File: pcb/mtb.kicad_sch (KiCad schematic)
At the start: 24 parts, among them J1 Screw_Terminal_01x04, J2 PROG/DEBUG, SW1 SW_MEC_5E, U1 AMS1117-3.3, U2 SN75176AP, Y1 Crystal

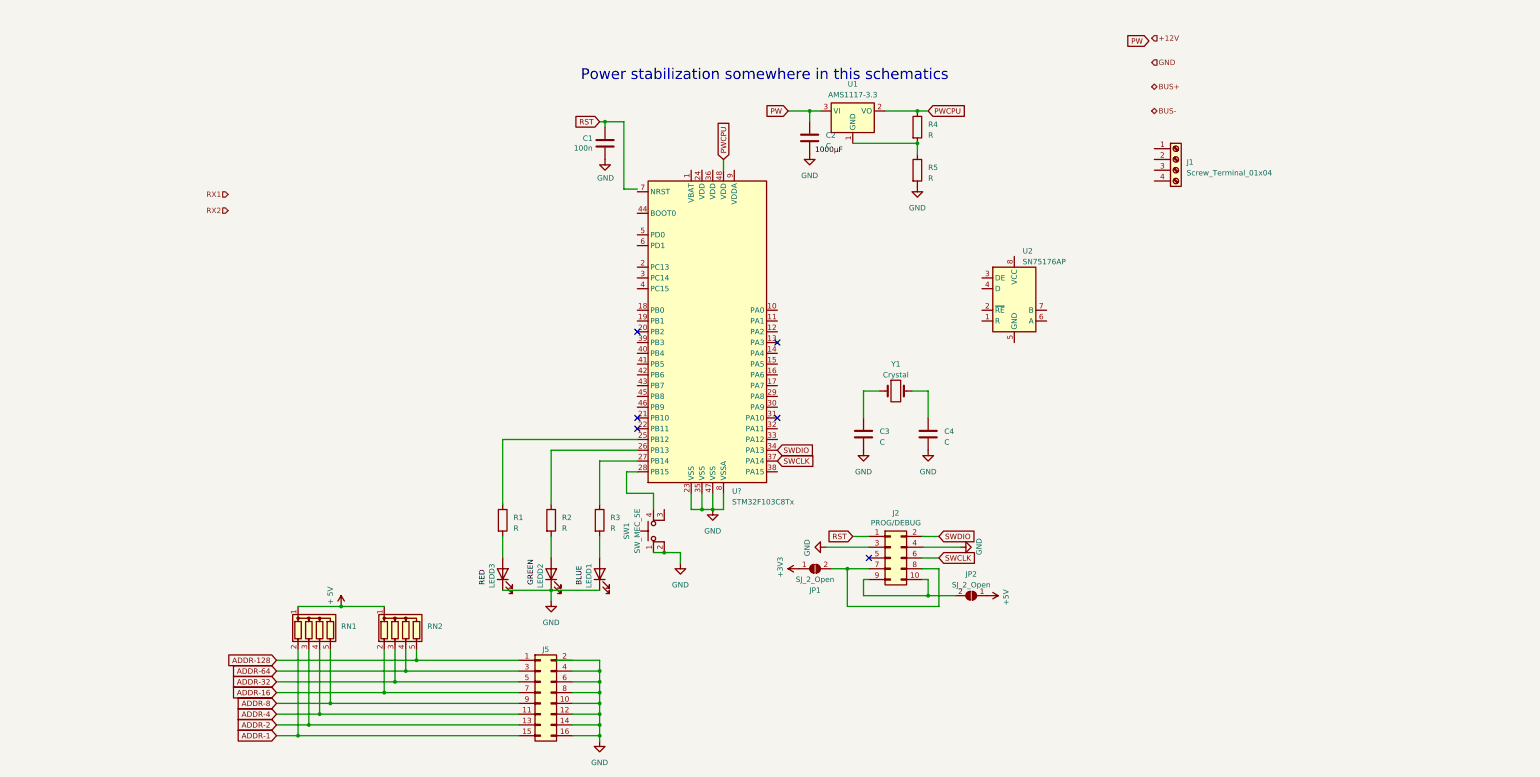
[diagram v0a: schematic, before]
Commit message: Wires adresses, add capacitors to MCU.
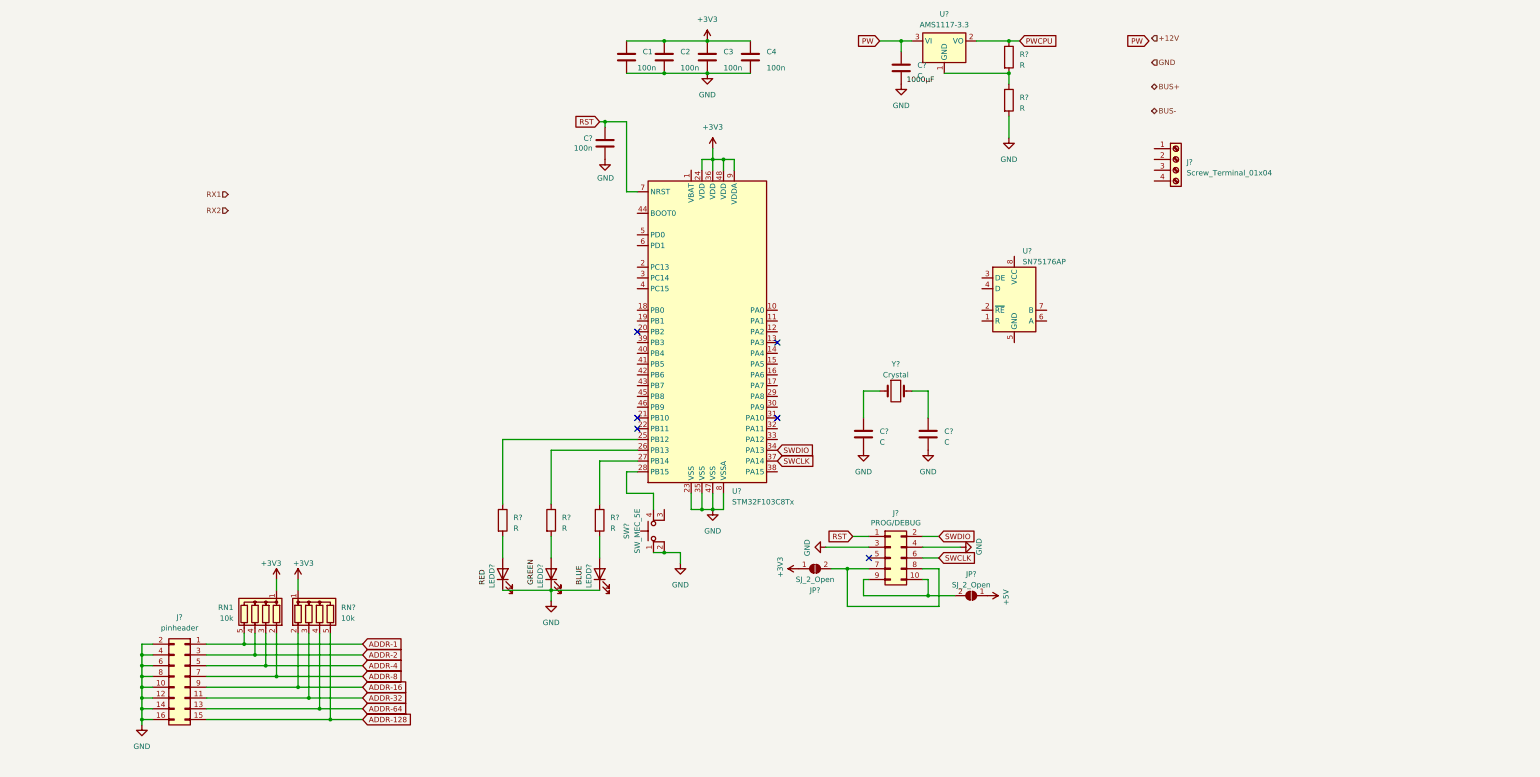
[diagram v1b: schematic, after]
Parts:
- removed RN2: R_Network04, Resistor_THT:R_Array_SIP5, symbol Device:R_Network04
- added C1, C2, C3, C4: 100n, symbol Device:C
- added RN?: 10k, Resistor_THT:R_Array_SIP5, symbol Device:R_Network04
- J?: renamed from J5; value ~ -> pinheader
- RN1: value R_Network04 -> 10k; footprint OptoDevice:R_LDR_5.1x4.3mm_P3.4mm_Vertical -> Resistor_THT:R_Array_SIP5
- renumbered C4 to C?, C2 to C?, C1 to C?, C3 to C?, D2 to D?, D3 to D?, D1 to D?, J2 to J?, J1 to J?, JP2 to JP?, JP1 to JP?, R2 to R?, R5 to R?, R4 to R?, R3 to R?, R1 to R?, SW1 to SW?, U2 to U?, U1 to U?, Y1 to Y?
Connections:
- net NEUT is gone; now on net +3V3: RN1.1 (common)
- net +3V3: now also U?.24 (VDD), U?.36 (VDD), U?.48 (VDD), U?.9 (VDDA), C1.1, C2.1, C3.1, C4.1, RN?.1 (common)
- net ADDR-1: now also J?.1 (Pin_1), RN1.5 (R4); no longer J?.15 (Pin_15), RN1.2 (R1)
- net ADDR-128: now also J?.15 (Pin_15), RN?.5 (R4); no longer J?.1 (Pin_1)
- net ADDR-16: now also J?.9 (Pin_9), RN?.2 (R1); no longer J?.7 (Pin_7)
- net ADDR-2: now also J?.3 (Pin_3), RN1.4 (R3); no longer J?.13 (Pin_13), RN1.3 (R2)
- net ADDR-32: now also J?.11 (Pin_11), RN?.3 (R2); no longer J?.5 (Pin_5)
- net ADDR-4: now also J?.5 (Pin_5), RN1.3 (R2); no longer J?.11 (Pin_11), RN1.4 (R3)
- net ADDR-64: now also J?.13 (Pin_13), RN?.4 (R3); no longer J?.3 (Pin_3)
- net ADDR-8: now also J?.7 (Pin_7), RN1.2 (R1); no longer J?.9 (Pin_9), RN1.5 (R4)
- net GND: now also J?.2 (Pin_2), C1.2, C2.2, C3.2, C4.2
- net PWCPU: no longer U?.48 (VDD)
- net RST: now also U?.7 (NRST)
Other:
- note removed: "Power stabilization somewhere in this schematics"
- moved on the sheet: C?, J?, R?, U?

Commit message: Add power supply.
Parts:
- removed C?: C, symbol Device:C
- removed J?: Screw_Terminal_01x04, symbol Connector:Screw_Terminal_01x04
- removed R? (x2): R, symbol Device:R
- added C5, C6: 100n, symbol Device:C
- added C7, C9: 22u, symbol Device:C
- added C8: 22u/25V, symbol Device:C
- added D1: D_Schottky, symbol Device:D_Schottky
- added D2: BZX84C18, Package_TO_SOT_SMD:SOT-23, symbol Diode:BZX84Cxx
- added D3: BT148, symbol Device:Q_SCR_KAG
- added F1: 200mA, symbol Device:Polyfuse
- added R1: 2k2, symbol Device:R
- added U1: L78L05_SOT89, Package_TO_SOT_SMD:SOT-89-3, symbol Regulator_Linear:L78L05_SOT89
- C? (x2): value C -> 22p
- Y?: value Crystal -> 8MHz
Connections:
- net PWCPU is gone; now on net +3V3: U?.2 (VO)
- net +12V: now also F1.2
- net +3V3: now also C7.2
- net +5V: now also C9.2, U1.1 (OUT)
- net GND: now also U?.1 (GND), C5.2, C6.2, C7.1, C8.2, C9.1, D3.1 (K), R1.2, U1.2 (GND)
- net at U?.5 (PD0): now also C?.1, Y?.2
- net at U?.6 (PD1): now also C?.1, Y?.1
- net PW: no longer names the net of U?.3 (VI)
- net PW: now also C8.1, D1.1 (K), D2.3 (K), D3.2 (A), U1.3 (IN)
- new net: C6.1, D2.1 (A), D3.3 (G), R1.1
- new net: C5.1, D1.2 (A), F1.1
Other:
- moved on the sheet: C1, C2, C3, C4, C?, D?, J?, JP?, R?, SW?, U?, Y?

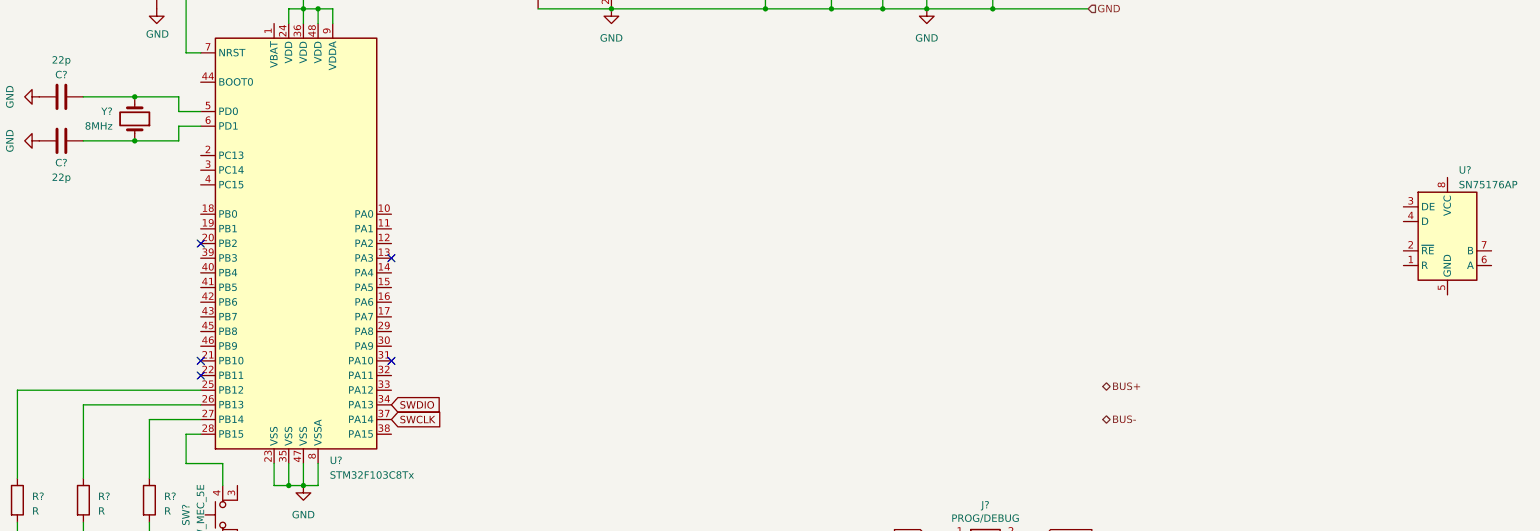
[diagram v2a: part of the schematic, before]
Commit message: Wire MTB bus driver.
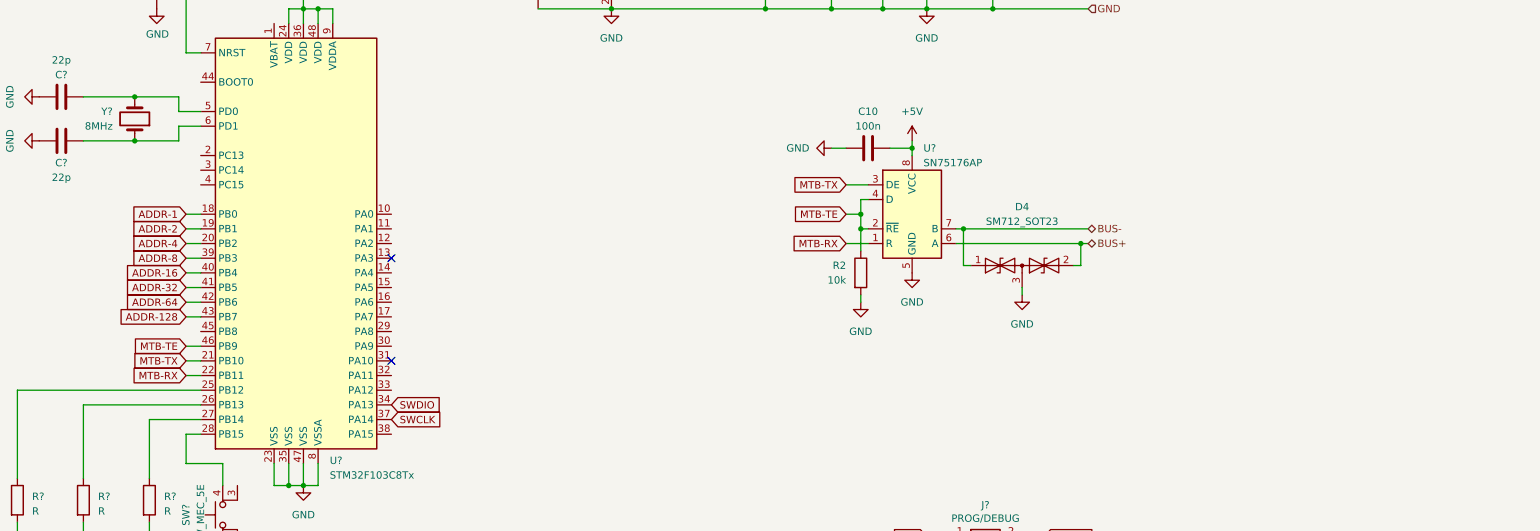
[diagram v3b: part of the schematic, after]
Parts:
- added C10: 100n, symbol Device:C
- added D4: SM712_SOT23, Package_TO_SOT_SMD:SOT-23, symbol Diode:SM712_SOT23
- added R2: 10k, symbol Device:R
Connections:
- net +5V: now also U?.8 (VCC), C10.1
- net ADDR-1: now also U?.18 (PB0)
- net ADDR-128: now also U?.43 (PB7)
- net ADDR-16: now also U?.40 (PB4)
- net ADDR-2: now also U?.19 (PB1)
- net ADDR-32: now also U?.41 (PB5)
- net ADDR-4: now also U?.20 (PB2)
- net ADDR-64: now also U?.42 (PB6)
- net ADDR-8: now also U?.39 (PB3)
- net BUS+: now also U?.6 (A), D4.2 (A2)
- net BUS-: now also U?.7 (B), D4.1 (A1)
- net GND: now also U?.5 (GND), C10.2, D4.3 (common), R2.2
- net MTB-TX: now reaches U?.21 (PB10)
- net MTB-TX: now also U?.3 (DE)
- net MTB-RX: now reaches U?.22 (PB11)
- net MTB-RX: now also U?.1 (R)
- net MTB-TE: now reaches U?.46 (PB9)
- net MTB-TE: now also U?.2 (~{RE}), U?.4 (D), R2.1
- no-connect marks 6 -> 3
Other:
- moved on the sheet: U?

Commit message: Finished MTB part.
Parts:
- added R2: 10k, symbol Device:R
- D1: renamed from D?; value LED -> BLUE
- D2: renamed from D?; value LED -> GREEN
- D3: renamed from D?; value LED -> RED
- R1, R3, R4: renamed from R?; value R -> 1k
- gave numbers to parts that had none: 13
- renumbered C4 to C1, C8 to C10, C10 to C11, C6 to C12, C5 to C13, C3 to C2, C2 to C3, C1 to C4, C9 to C8, C7 to C9, D3 to D4, D2 to D5, D1 to D6, D4 to D7, R2 to R5, R1 to R6, RN1 to RN2, U1 to U10
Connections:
- net GND: now also R2.2
- net RX1: now also U8.31 (PA10)
- net RX2: now also U8.13 (PA3)
- net DCC: now reaches U8.10 (PA0)
- net MULT1: now reaches U8.11 (PA1)
- net MULT2: now reaches U8.12 (PA2)
- net at U8.44 (BOOT0): now also R2.1
- no-connect marks 3 -> 16
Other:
- company: (none) -> Laboratory of railway vehicles control
- title: (none) -> RailComDet - MTB part
- moved on the sheet: C1, C11, C2, C3, C4, C5, C6, C7, D1, D2, D3, D7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

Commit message: DCC WIP.
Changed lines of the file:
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@@
     )
   )
-  (global_label "ADDR-16" (shape input) (at 218.44 144.78 180) (fields_autoplaced)
+  (global_label "ADDR-16" (shape output) (at 218.44 144.78 180) (fields_autoplaced)
     (effects (font (size 1.27 1.27)) (justify right))
-    (property "Intersheetrefs" "${INTERSHEET_REFS}" (at 206.6442 144.78 0)
+    (property "Intersheetrefs" "${INTERSHEET_REFS}" (at 206.5648 144.78 0)
       (effects (font (size 1.27 1.27)) (justify right) hide)
     )
@@
     )
   )
-  (global_label "ADDR-128" (shape input) (at 218.44 152.4 180) (fields_autoplaced)
+  (global_label "ADDR-128" (shape output) (at 218.44 152.4 180) (fields_autoplaced)
     (effects (font (size 1.27 1.27)) (justify right))
-    (property "Intersheetrefs" "${INTERSHEET_REFS}" (at 205.4347 152.4 0)
+    (property "Intersheetrefs" "${INTERSHEET_REFS}" (at 205.3553 152.4 0)
       (effects (font (size 1.27 1.27)) (justify right) hide)
     )
@@
     )
   )
-  (global_label "MTB-TX" (shape input) (at 88.9 113.03 0) (fields_autoplaced)
+  (global_label "MTB-TX" (shape output) (at 88.9 113.03 0) (fields_autoplaced)
     (effects (font (size 1.27 1.27)) (justify left))
     (property "Intersheetrefs" "${INTERSHEET_REFS}" (at 99.3237 113.03 0)
@@
     )
   )
-  (global_label "ADDR-1" (shape input) (at 218.44 134.62 180) (fields_autoplaced)
+  (global_label "ADDR-1" (shape output) (at 218.44 134.62 180) (fields_autoplaced)
     (effects (font (size 1.27 1.27)) (justify right))
-    (property "Intersheetrefs" "${INTERSHEET_REFS}" (at 207.8537 134.62 0)
+    (property "Intersheetrefs" "${INTERSHEET_REFS}" (at 207.7743 134.62 0)
       (effects (font (size 1.27 1.27)) (justify right) hide)
     )
@@
     )
   )
-  (global_label "ADDR-2" (shape input) (at 218.44 137.16 180) (fields_autoplaced)
+  (global_label "ADDR-2" (shape output) (at 218.44 137.16 180) (fields_autoplaced)
     (effects (font (size 1.27 1.27)) (justify right))
-    (property "Intersheetrefs" "${INTERSHEET_REFS}" (at 207.8537 137.16 0)
+    (property "Intersheetrefs" "${INTERSHEET_REFS}" (at 207.7743 137.16 0)
       (effects (font (size 1.27 1.27)) (justify right) hide)
     )
@@
     )
   )
-  (global_label "ADDR-32" (shape input) (at 218.44 147.32 180) (fields_autoplaced)
+  (global_label "ADDR-32" (shape output) (at 218.44 147.32 180) (fields_autoplaced)
     (effects (font (size 1.27 1.27)) (justify right))
-    (property "Intersheetrefs" "${INTERSHEET_REFS}" (at 206.6442 147.32 0)
+    (property "Intersheetrefs" "${INTERSHEET_REFS}" (at 206.5648 147.32 0)
       (effects (font (size 1.27 1.27)) (justify right) hide)
     )
@@
     )
   )
-  (global_label "MTB-TE" (shape input) (at 88.9 110.49 0) (fields_autoplaced)
+  (global_label "MTB-TE" (shape output) (at 88.9 110.49 0) (fields_autoplaced)
     (effects (font (size 1.27 1.27)) (justify left))
     (property "Intersheetrefs" "${INTERSHEET_REFS}" (at 99.2632 110.49 0)
@@
     )
   )
-  (global_label "ADDR-64" (shape input) (at 218.44 149.86 180) (fields_autoplaced)
+  (global_label "ADDR-64" (shape output) (at 218.44 149.86 180) (fields_autoplaced)
     (effects (font (size 1.27 1.27)) (justify right))
-    (property "Intersheetrefs" "${INTERSHEET_REFS}" (at 206.6442 149.86 0)
+    (property "Intersheetrefs" "${INTERSHEET_REFS}" (at 206.5648 149.86 0)
       (effects (font (size 1.27 1.27)) (justify right) hide)
     )
   )
-  (global_label "MTB-RX" (shape input) (at 227.33 91.44 180) (fields_autoplaced)
+  (global_label "MTB-RX" (shape output) (at 227.33 91.44 180) (fields_autoplaced)
     (effects (font (size 1.27 1.27)) (justify right))
     (property "Intersheetrefs" "${INTERSHEET_REFS}" (at 216.6039 91.44 0)
@@
     )
   )
-  (global_label "ADDR-4" (shape input) (at 218.44 139.7 180) (fields_autoplaced)
+  (global_label "ADDR-4" (shape output) (at 218.44 139.7 180) (fields_autoplaced)
     (effects (font (size 1.27 1.27)) (justify right))
-    (property "Intersheetrefs" "${INTERSHEET_REFS}" (at 207.8537 139.7 0)
+    (property "Intersheetrefs" "${INTERSHEET_REFS}" (at 207.7743 139.7 0)
       (effects (font (size 1.27 1.27)) (justify right) hide)
     )
@@
     )
   )
-  (global_label "ADDR-8" (shape input) (at 218.44 142.24 180) (fields_autoplaced)
+  (global_label "ADDR-8" (shape output) (at 218.44 142.24 180) (fields_autoplaced)
     (effects (font (size 1.27 1.27)) (justify right))
-    (property "Intersheetrefs" "${INTERSHEET_REFS}" (at 207.8537 142.24 0)
+    (property "Intersheetrefs" "${INTERSHEET_REFS}" (at 207.7743 142.24 0)
       (effects (font (size 1.27 1.27)) (justify right) hide)
     )

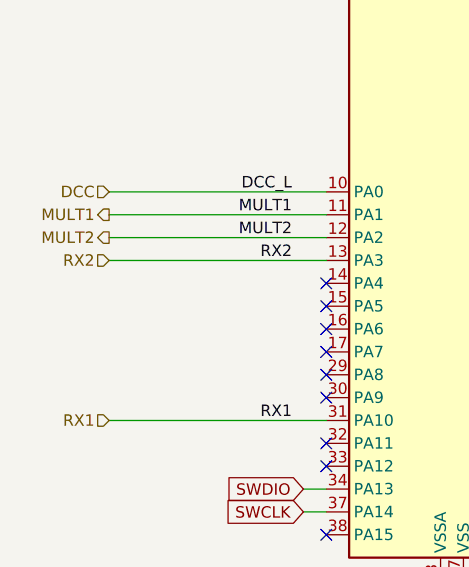
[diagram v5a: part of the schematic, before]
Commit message: Connect DCC and MTB parts.
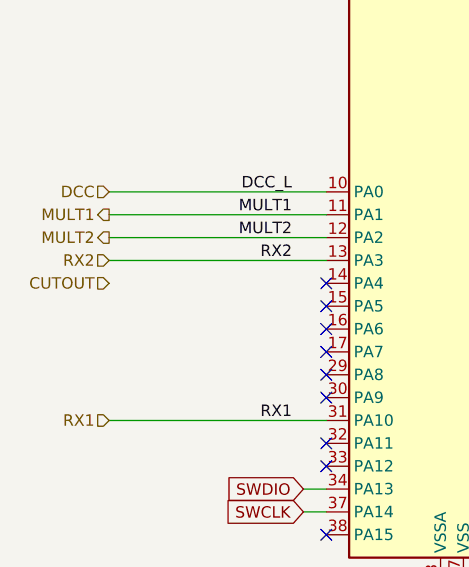
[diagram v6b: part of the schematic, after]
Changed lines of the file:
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@@
+    (effects (font (size 1.27 1.27)) (justify right))
+  )
+  (hierarchical_label "CUTOUT" (shape input) (at 29.21 97.79 180) (fields_autoplaced)
     (effects (font (size 1.27 1.27)) (justify right))
   )

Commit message: Finished.
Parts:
- Y1: value 8MHz -> 14,7456MHz
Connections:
- net CUTOUT: now also U8.14 (PA4)
- no-connect marks 16 -> 15
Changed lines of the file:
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@@
   (no_connect (at 69.85 176.53))
   (no_connect (at 73.66 54.61))
-  (no_connect (at 53.34 97.79))
   (no_connect (at 86.36 107.95))
   (no_connect (at 53.34 118.11))
@@
     (stroke (width 0) (type default))
   )
+  (wire (pts (xy 29.21 97.79) (xy 53.34 97.79))
+    (stroke (width 0) (type default))
+  )
   (wire (pts (xy 229.87 88.9) (xy 231.14 88.9))
     (stroke (width 0) (type default))
@@
   )
   (label "RX1" (at 49.53 113.03 180) (fields_autoplaced)
+    (effects (font (size 1.27 1.27)) (justify right bottom))
+  )
+  (label "CUTOUT" (at 49.53 97.79 180) (fields_autoplaced)
     (effects (font (size 1.27 1.27)) (justify right bottom))
   )
@@
       (effects (font (size 1.27 1.27)) (justify right))
     )
-    (property "Value" "8MHz" (at 101.6 72.39 90)
+    (property "Value" "14,7456MHz" (at 95.25 76.2 90)
       (effects (font (size 1.27 1.27)) (justify right))
     )
